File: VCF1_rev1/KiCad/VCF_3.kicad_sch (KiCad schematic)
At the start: 20 parts, among them U10 CEM3350, U13 74HC4053, U14 Opamp_Quad

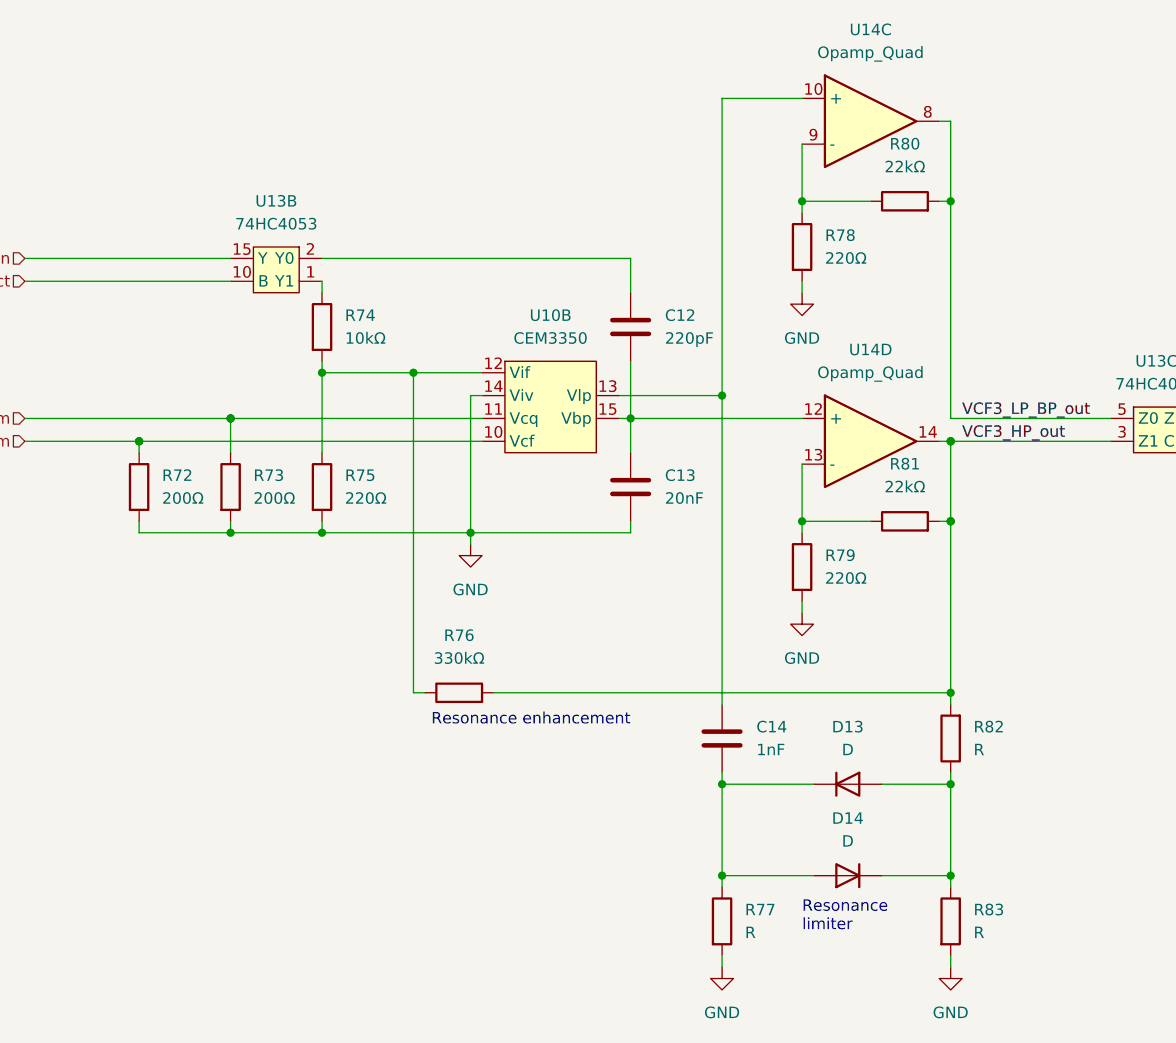
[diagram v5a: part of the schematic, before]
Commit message: Cleaned up the first page with the overview and tried to make it a bit more readable.
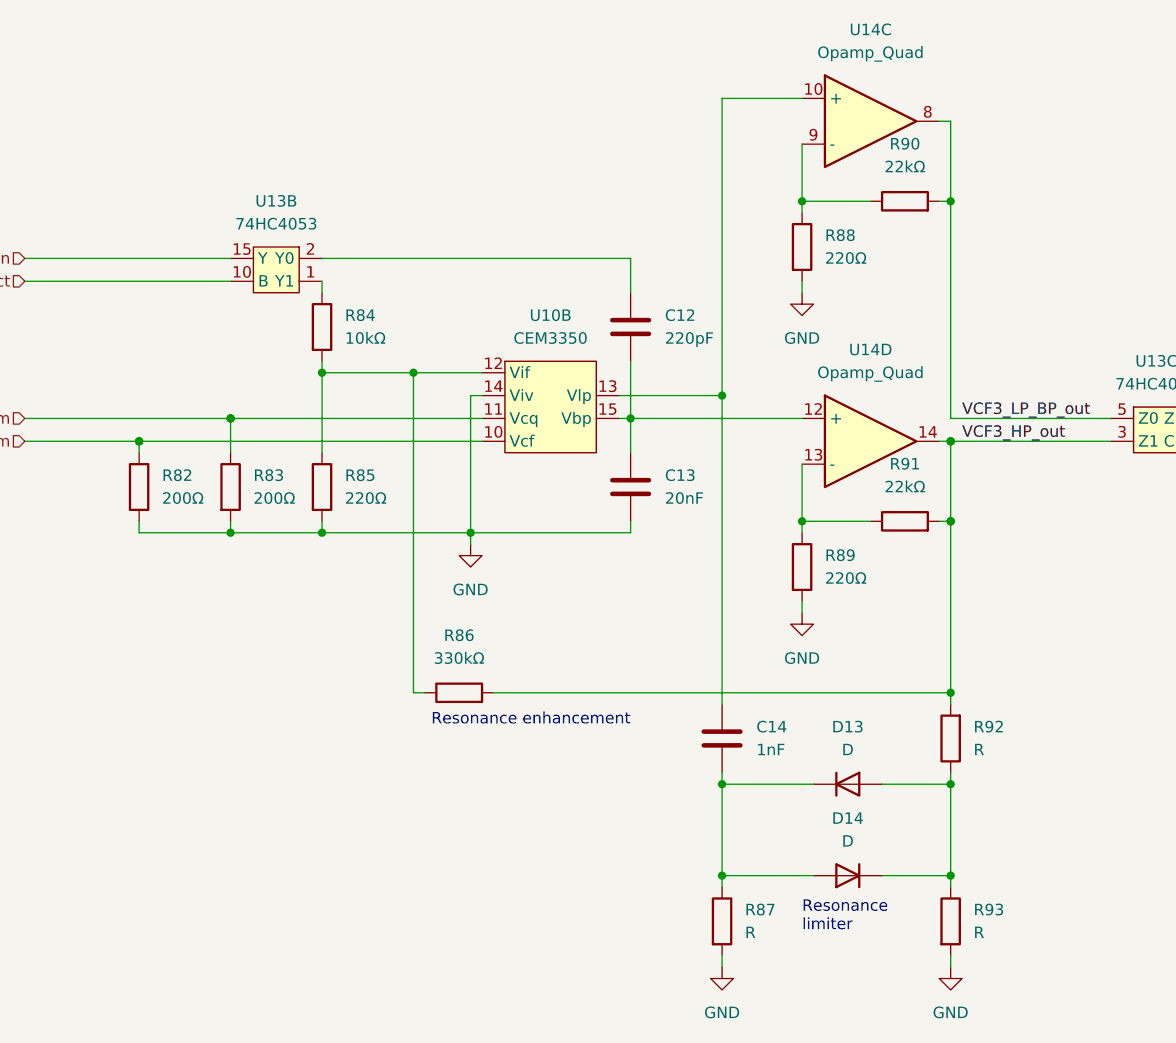
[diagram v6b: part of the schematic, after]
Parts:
- renumbered R72 to R82, R73 to R83, R74 to R84, R75 to R85, R76 to R86, R77 to R87, R78 to R88, R79 to R89, R80 to R90, R81 to R91, R82 to R92, R83 to R93
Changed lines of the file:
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@@
 (kicad_sch (version 20210621) (generator eeschema)
   (paper "A4")
-  (junction (at 149.86 143.51) (diameter 0) (color 0 0 0 0))
-  (junction (at 96.52 115.57) (diameter 0) (color 0 0 0 0))
-  (junction (at 124.46 153.67) (diameter 0) (color 0 0 0 0))
   (junction (at 149.86 114.3001) (diameter 0) (color 0 0 0 0))
-  (junction (at 149.86 133.35) (diameter 0) (color 0 0 0 0))
-  (junction (at 80.01 115.5701) (diameter 0) (color 0 0 0 0))
-  (junction (at 59.69 105.41) (diameter 0) (color 0 0 0 0))
-  (junction (at 69.85 115.5701) (diameter 0) (color 0 0 0 0))
-  (junction (at 149.86 105.41) (diameter 0) (color 0 0 0 0))
-  (junction (at 114.3 102.87) (diameter 0) (color 0 0 0 0))
   (junction (at 149.86 114.3) (diameter 0) (color 0 0 0 0))
   (junction (at 149.86 78.7401) (diameter 0) (color 0 0 0 0))
-  (junction (at 59.69 105.4101) (diameter 0) (color 0 0 0 0))
-  (junction (at 90.17 97.79) (diameter 0) (color 0 0 0 0))
+  (junction (at 124.46 100.33) (diameter 0) (color 0 0 0 0))
+  (junction (at 69.85 102.8701) (diameter 0) (color 0 0 0 0))
   (junction (at 124.46 143.51) (diameter 0) (color 0 0 0 0))
-  (junction (at 149.86 105.4101) (diameter 0) (color 0 0 0 0))
-  (junction (at 69.85 102.8701) (diameter 0) (color 0 0 0 0))
-  (junction (at 149.86 153.67) (diameter 0) (color 0 0 0 0))
-  (junction (at 124.46 100.33) (diameter 0) (color 0 0 0 0))
+  (junction (at 80.01 115.5701) (diameter 0) (color 0 0 0 0))
+  (junction (at 133.35 114.3001) (diameter 0) (color 0 0 0 0))
+  (junction (at 149.86 105.41) (diameter 0) (color 0 0 0 0))
+  (junction (at 124.46 153.67) (diameter 0) (color 0 0 0 0))
+  (junction (at 133.35 78.7401) (diameter 0) (color 0 0 0 0))
   (junction (at 80.01 97.7901) (diameter 0) (color 0 0 0 0))
   (junction (at 69.85 102.87) (diameter 0) (color 0 0 0 0))
-  (junction (at 133.35 114.3001) (diameter 0) (color 0 0 0 0))
-  (junction (at 133.35 78.7401) (diameter 0) (color 0 0 0 0))
+  (junction (at 59.69 105.4101) (diameter 0) (color 0 0 0 0))
+  (junction (at 114.3 102.87) (diameter 0) (color 0 0 0 0))
+  (junction (at 69.85 115.5701) (diameter 0) (color 0 0 0 0))
+  (junction (at 96.52 115.57) (diameter 0) (color 0 0 0 0))
+  (junction (at 90.17 97.79) (diameter 0) (color 0 0 0 0))
+  (junction (at 149.86 153.67) (diameter 0) (color 0 0 0 0))
+  (junction (at 149.86 105.4101) (diameter 0) (color 0 0 0 0))
+  (junction (at 149.86 143.51) (diameter 0) (color 0 0 0 0))
+  (junction (at 59.69 105.41) (diameter 0) (color 0 0 0 0))
+  (junction (at 149.86 133.35) (diameter 0) (color 0 0 0 0))
   (wire (pts (xy 46.99 102.87) (xy 69.85 102.87))
     (stroke (width 0) (type default) (color 0 0 0 0))
@@
     (stroke (width 0) (type default) (color 0 0 0 0))
   )
+  (wire (pts (xy 149.86 78.7401) (xy 149.86 102.87))
+    (stroke (width 0) (type default) (color 0 0 0 0))
+  )
   (wire (pts (xy 149.86 69.8501) (xy 149.86 78.7401))
-    (stroke (width 0) (type default) (color 0 0 0 0))
-  )
-  (wire (pts (xy 149.86 78.7401) (xy 149.86 102.87))
     (stroke (width 0) (type default) (color 0 0 0 0))
   )
@@
   (symbol (lib_id "Device:R") (at 149.86 158.75 0) (unit 1)
     (in_bom yes) (on_board yes) (fields_autoplaced)
-    (property "Reference" "R83" (id 0) (at 152.4 157.4799 0)
+    (property "Reference" "R93" (id 0) (at 152.4 157.4799 0)
       (effects (font (size 1.27 1.27)) (justify left))
     )
@@
   (symbol (lib_id "Device:R") (at 133.35 119.3801 0) (unit 1)
     (in_bom yes) (on_board yes) (fields_autoplaced)
-    (property "Reference" "R79" (id 0) (at 135.89 118.11 0)
+    (property "Reference" "R89" (id 0) (at 135.89 118.11 0)
       (effects (font (size 1.27 1.27)) (justify left))
     )
@@
   (symbol (lib_id "Device:R") (at 144.78 78.7401 90) (unit 1)
     (in_bom yes) (on_board yes) (fields_autoplaced)
-    (property "Reference" "R80" (id 0) (at 144.78 72.3901 90))
+    (property "Reference" "R90" (id 0) (at 144.78 72.3901 90))
     (property "Value" "22kΩ" (id 1) (at 144.78 74.9301 90))
     (property "Footprint" "" (id 2) (at 144.78 80.5181 90)
@@
   (symbol (lib_id "power:GND") (at 96.52 116.84 0) (unit 1)
     (in_bom yes) (on_board yes) (fields_autoplaced)
-    (property "Reference" "#PWR031" (id 0) (at 96.52 123.19 0)
+    (property "Reference" "#PWR041" (id 0) (at 96.52 123.19 0)
       (effects (font (size 1.27 1.27)) hide)
     )
@@
   (symbol (lib_id "Device:R") (at 59.69 110.4901 0) (unit 1)
     (in_bom yes) (on_board yes)
-    (property "Reference" "R72" (id 0) (at 62.23 109.22 0)
+    (property "Reference" "R82" (id 0) (at 62.23 109.22 0)
       (effects (font (size 1.27 1.27)) (justify left))
     )
@@
   (symbol (lib_id "power:GND") (at 149.86 163.83 0) (unit 1)
     (in_bom yes) (on_board yes) (fields_autoplaced)
-    (property "Reference" "#PWR035" (id 0) (at 149.86 170.18 0)
+    (property "Reference" "#PWR045" (id 0) (at 149.86 170.18 0)
       (effects (font (size 1.27 1.27)) hide)
     )
@@
   (symbol (lib_id "power:GND") (at 133.35 88.9001 0) (unit 1)
     (in_bom yes) (on_board yes) (fields_autoplaced)
-    (property "Reference" "#PWR033" (id 0) (at 133.35 95.2501 0)
+    (property "Reference" "#PWR043" (id 0) (at 133.35 95.2501 0)
       (effects (font (size 1.27 1.27)) hide)
     )
@@
   (symbol (lib_id "Device:R") (at 80.01 92.71 0) (unit 1)
     (in_bom yes) (on_board yes) (fields_autoplaced)
-    (property "Reference" "R74" (id 0) (at 82.55 91.4399 0)
+    (property "Reference" "R84" (id 0) (at 82.55 91.4399 0)
       (effects (font (size 1.27 1.27)) (justify left))
     )
@@
   (symbol (lib_id "Device:R") (at 124.46 158.75 0) (unit 1)
     (in_bom yes) (on_board yes) (fields_autoplaced)
-    (property "Reference" "R77" (id 0) (at 127 157.4799 0)
+    (property "Reference" "R87" (id 0) (at 127 157.4799 0)
       (effects (font (size 1.27 1.27)) (justify left))
     )
@@
   (symbol (lib_id "Device:R") (at 144.78 114.3001 90) (unit 1)
     (in_bom yes) (on_board yes) (fields_autoplaced)
-    (property "Reference" "R81" (id 0) (at 144.78 107.9501 90))
+    (property "Reference" "R91" (id 0) (at 144.78 107.9501 90))
     (property "Value" "22kΩ" (id 1) (at 144.78 110.4901 90))
     (property "Footprint" "" (id 2) (at 144.78 116.0781 90)
@@
   (symbol (lib_id "Device:R") (at 133.35 83.8201 0) (unit 1)
     (in_bom yes) (on_board yes) (fields_autoplaced)
-    (property "Reference" "R78" (id 0) (at 135.89 82.55 0)
+    (property "Reference" "R88" (id 0) (at 135.89 82.55 0)
       (effects (font (size 1.27 1.27)) (justify left))
     )
@@
   (symbol (lib_id "Device:R") (at 149.86 138.43 180) (unit 1)
     (in_bom yes) (on_board yes) (fields_autoplaced)
-    (property "Reference" "R82" (id 0) (at 152.4 137.1599 0)
+    (property "Reference" "R92" (id 0) (at 152.4 137.1599 0)
       (effects (font (size 1.27 1.27)) (justify right))
     )
@@
   (symbol (lib_id "Device:R") (at 95.25 133.35 90) (unit 1)
     (in_bom yes) (on_board yes) (fields_autoplaced)
-    (property "Reference" "R76" (id 0) (at 95.25 127 90))
+    (property "Reference" "R86" (id 0) (at 95.25 127 90))
     (property "Value" "330kΩ" (id 1) (at 95.25 129.54 90))
     (property "Footprint" "" (id 2) (at 95.25 135.128 90)
@@
   (symbol (lib_id "Device:R") (at 80.01 110.4901 0) (unit 1)
     (in_bom yes) (on_board yes) (fields_autoplaced)
-    (property "Reference" "R75" (id 0) (at 82.55 109.22 0)
+    (property "Reference" "R85" (id 0) (at 82.55 109.22 0)
       (effects (font (size 1.27 1.27)) (justify left))
     )
@@
   (symbol (lib_id "power:GND") (at 133.35 124.4601 0) (unit 1)
     (in_bom yes) (on_board yes) (fields_autoplaced)
-    (property "Reference" "#PWR034" (id 0) (at 133.35 130.8101 0)
+    (property "Reference" "#PWR044" (id 0) (at 133.35 130.8101 0)
       (effects (font (size 1.27 1.27)) hide)
     )
@@
   (symbol (lib_id "power:GND") (at 124.46 163.83 0) (unit 1)
     (in_bom yes) (on_board yes) (fields_autoplaced)
-    (property "Reference" "#PWR032" (id 0) (at 124.46 170.18 0)
+    (property "Reference" "#PWR042" (id 0) (at 124.46 170.18 0)
       (effects (font (size 1.27 1.27)) hide)
     )
@@
   (symbol (lib_id "Device:R") (at 69.85 110.4901 0) (unit 1)
     (in_bom yes) (on_board yes)
-    (property "Reference" "R73" (id 0) (at 72.39 109.22 0)
-      (effects (font (size 1.27 1.27)) (justify left))
-    )
+    (property "Reference" "R83" (id 0) (at 72.39 109.22 0)
+      (effects (font (size 1.27 1.27)) (justify left))
+    )

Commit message: Drew a better symbol for LM13700 because the other one was ugly.
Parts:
- R82, R83, R84, R85, R86, R87, R88, R89, R90, R91, R92, R93: footprint (none) -> Resistor_SMD:R_0603_1608Metric
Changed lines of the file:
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@@
 (kicad_sch (version 20210621) (generator eeschema)
   (paper "A4")
+  (junction (at 149.86 143.51) (diameter 0) (color 0 0 0 0))
+  (junction (at 124.46 153.67) (diameter 0) (color 0 0 0 0))
+  (junction (at 114.3 102.87) (diameter 0) (color 0 0 0 0))
+  (junction (at 149.86 153.67) (diameter 0) (color 0 0 0 0))
+  (junction (at 124.46 100.33) (diameter 0) (color 0 0 0 0))
+  (junction (at 149.86 133.35) (diameter 0) (color 0 0 0 0))
+  (junction (at 133.35 114.3001) (diameter 0) (color 0 0 0 0))
+  (junction (at 80.01 115.5701) (diameter 0) (color 0 0 0 0))
   (junction (at 149.86 114.3001) (diameter 0) (color 0 0 0 0))
+  (junction (at 149.86 78.7401) (diameter 0) (color 0 0 0 0))
+  (junction (at 96.52 115.57) (diameter 0) (color 0 0 0 0))
+  (junction (at 69.85 115.5701) (diameter 0) (color 0 0 0 0))
+  (junction (at 124.46 143.51) (diameter 0) (color 0 0 0 0))
+  (junction (at 59.69 105.41) (diameter 0) (color 0 0 0 0))
+  (junction (at 69.85 102.8701) (diameter 0) (color 0 0 0 0))
+  (junction (at 149.86 105.41) (diameter 0) (color 0 0 0 0))
+  (junction (at 80.01 97.7901) (diameter 0) (color 0 0 0 0))
   (junction (at 149.86 114.3) (diameter 0) (color 0 0 0 0))
-  (junction (at 149.86 78.7401) (diameter 0) (color 0 0 0 0))
-  (junction (at 124.46 100.33) (diameter 0) (color 0 0 0 0))
-  (junction (at 69.85 102.8701) (diameter 0) (color 0 0 0 0))
-  (junction (at 124.46 143.51) (diameter 0) (color 0 0 0 0))
-  (junction (at 80.01 115.5701) (diameter 0) (color 0 0 0 0))
-  (junction (at 133.35 114.3001) (diameter 0) (color 0 0 0 0))
-  (junction (at 149.86 105.41) (diameter 0) (color 0 0 0 0))
-  (junction (at 124.46 153.67) (diameter 0) (color 0 0 0 0))
-  (junction (at 133.35 78.7401) (diameter 0) (color 0 0 0 0))
-  (junction (at 80.01 97.7901) (diameter 0) (color 0 0 0 0))
   (junction (at 69.85 102.87) (diameter 0) (color 0 0 0 0))
   (junction (at 59.69 105.4101) (diameter 0) (color 0 0 0 0))
-  (junction (at 114.3 102.87) (diameter 0) (color 0 0 0 0))
-  (junction (at 69.85 115.5701) (diameter 0) (color 0 0 0 0))
-  (junction (at 96.52 115.57) (diameter 0) (color 0 0 0 0))
   (junction (at 90.17 97.79) (diameter 0) (color 0 0 0 0))
-  (junction (at 149.86 153.67) (diameter 0) (color 0 0 0 0))
+  (junction (at 133.35 78.7401) (diameter 0) (color 0 0 0 0))
   (junction (at 149.86 105.4101) (diameter 0) (color 0 0 0 0))
-  (junction (at 149.86 143.51) (diameter 0) (color 0 0 0 0))
-  (junction (at 59.69 105.41) (diameter 0) (color 0 0 0 0))
-  (junction (at 149.86 133.35) (diameter 0) (color 0 0 0 0))
   (wire (pts (xy 46.99 102.87) (xy 69.85 102.87))
     (stroke (width 0) (type default) (color 0 0 0 0))
@@
     (stroke (width 0) (type default) (color 0 0 0 0))
   )
+  (wire (pts (xy 149.86 69.8501) (xy 149.86 78.7401))
+    (stroke (width 0) (type default) (color 0 0 0 0))
+  )
   (wire (pts (xy 149.86 78.7401) (xy 149.86 102.87))
-    (stroke (width 0) (type default) (color 0 0 0 0))
-  )
-  (wire (pts (xy 149.86 69.8501) (xy 149.86 78.7401))
     (stroke (width 0) (type default) (color 0 0 0 0))
   )
@@
       (effects (font (size 1.27 1.27)) (justify left))
     )
-    (property "Footprint" "" (id 2) (at 148.082 158.75 90)
+    (property "Footprint" "Resistor_SMD:R_0603_1608Metric" (id 2) (at 148.082 158.75 90)
       (effects (font (size 1.27 1.27)) hide)
     )
@@
       (effects (font (size 1.27 1.27)) (justify left))
     )
-    (property "Footprint" "" (id 2) (at 131.572 119.3801 90)
+    (property "Footprint" "Resistor_SMD:R_0603_1608Metric" (id 2) (at 131.572 119.3801 90)
       (effects (font (size 1.27 1.27)) hide)
     )
@@
     (property "Reference" "R90" (id 0) (at 144.78 72.3901 90))
     (property "Value" "22kΩ" (id 1) (at 144.78 74.9301 90))
-    (property "Footprint" "" (id 2) (at 144.78 80.5181 90)
+    (property "Footprint" "Resistor_SMD:R_0603_1608Metric" (id 2) (at 144.78 80.5181 90)
       (effects (font (size 1.27 1.27)) hide)
     )
@@
       (effects (font (size 1.27 1.27)) (justify left))
     )
-    (property "Footprint" "" (id 2) (at 57.912 110.4901 90)
+    (property "Footprint" "Resistor_SMD:R_0603_1608Metric" (id 2) (at 57.912 110.4901 90)
       (effects (font (size 1.27 1.27)) hide)
     )
@@
       (effects (font (size 1.27 1.27)) (justify left))
     )
-    (property "Footprint" "" (id 2) (at 78.232 92.71 90)
+    (property "Footprint" "Resistor_SMD:R_0603_1608Metric" (id 2) (at 78.232 92.71 90)
       (effects (font (size 1.27 1.27)) hide)
     )
@@
       (effects (font (size 1.27 1.27)) (justify left))
     )
-    (property "Footprint" "" (id 2) (at 122.682 158.75 90)
+    (property "Footprint" "Resistor_SMD:R_0603_1608Metric" (id 2) (at 122.682 158.75 90)
       (effects (font (size 1.27 1.27)) hide)
     )
@@
     (property "Reference" "R91" (id 0) (at 144.78 107.9501 90))
     (property "Value" "22kΩ" (id 1) (at 144.78 110.4901 90))
-    (property "Footprint" "" (id 2) (at 144.78 116.0781 90)
+    (property "Footprint" "Resistor_SMD:R_0603_1608Metric" (id 2) (at 144.78 116.0781 90)
       (effects (font (size 1.27 1.27)) hide)
     )
@@
       (effects (font (size 1.27 1.27)) (justify left))
     )
-    (property "Footprint" "" (id 2) (at 131.572 83.8201 90)
+    (property "Footprint" "Resistor_SMD:R_0603_1608Metric" (id 2) (at 131.572 83.8201 90)
       (effects (font (size 1.27 1.27)) hide)
     )
@@
       (effects (font (size 1.27 1.27)) (justify right))
     )
-    (property "Footprint" "" (id 2) (at 151.638 138.43 90)
+    (property "Footprint" "Resistor_SMD:R_0603_1608Metric" (id 2) (at 151.638 138.43 90)
       (effects (font (size 1.27 1.27)) hide)
     )
@@
     (property "Reference" "R86" (id 0) (at 95.25 127 90))
     (property "Value" "330kΩ" (id 1) (at 95.25 129.54 90))
-    (property "Footprint" "" (id 2) (at 95.25 135.128 90)
+    (property "Footprint" "Resistor_SMD:R_0603_1608Metric" (id 2) (at 95.25 135.128 90)
       (effects (font (size 1.27 1.27)) hide)
     )
@@
       (effects (font (size 1.27 1.27)) (justify left))
     )
-    (property "Footprint" "" (id 2) (at 78.232 110.4901 90)
+    (property "Footprint" "Resistor_SMD:R_0603_1608Metric" (id 2) (at 78.232 110.4901 90)
       (effects (font (size 1.27 1.27)) hide)
     )
@@
       (effects (font (size 1.27 1.27)) (justify left))
     )
-    (property "Footprint" "" (id 2) (at 68.072 110.4901 90)
-      (effects (font (size 1.27 1.27)) hide)
-    )
+    (property "Footprint" "Resistor_SMD:R_0603_1608Metric" (id 2) (at 68.072 110.4901 90)
+      (effects (font (size 1.27 1.27)) hide)
+    )
